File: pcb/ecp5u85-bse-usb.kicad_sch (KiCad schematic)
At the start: 25 parts, among them J1 Conn_02x40_Odd_Even, J2 Conn_02x40_Odd_Even

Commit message: Fix some ERC errors
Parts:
- gave numbers to parts that had none: 23
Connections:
- net +2V5: now also R33.1
- no-connect marks 15 -> 16

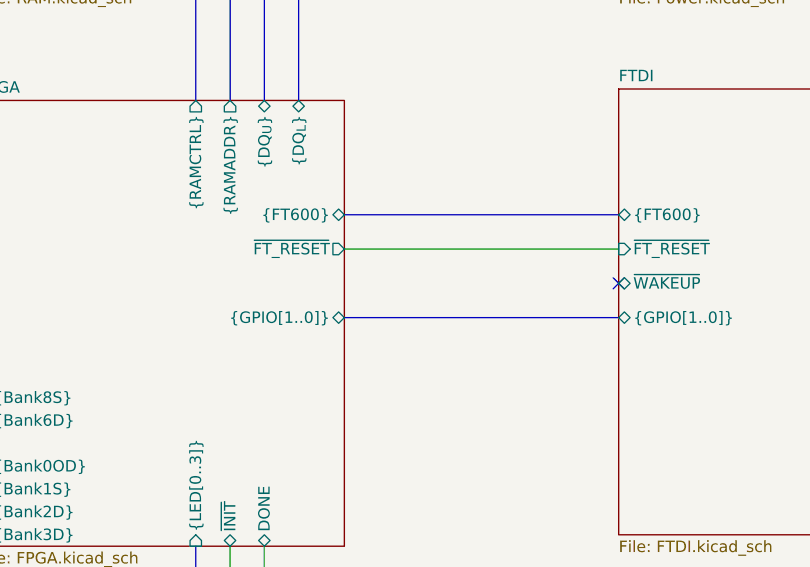
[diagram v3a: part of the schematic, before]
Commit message: Conect FT_WAKEUP and move FT_RESET to an optional circuit
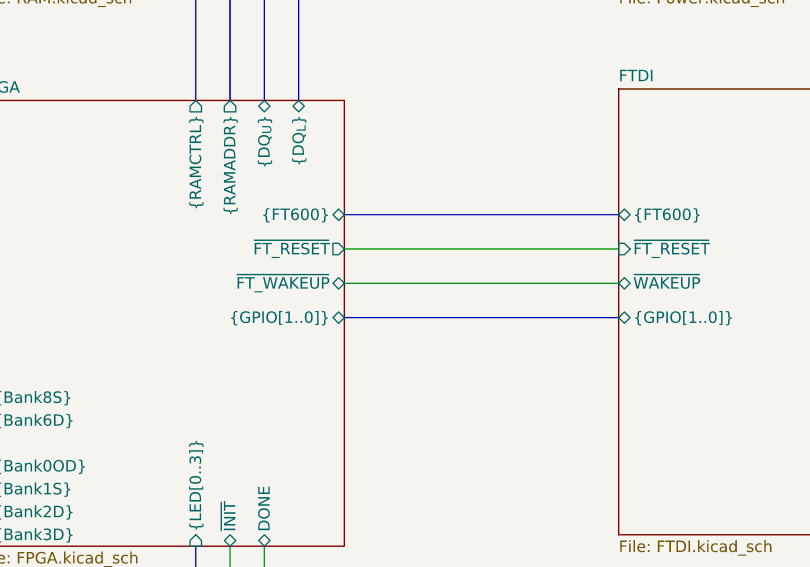
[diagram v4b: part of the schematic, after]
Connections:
- no-connect marks 16 -> 15
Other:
- sheet FPGA ports: added ~{FT_WAKEUP}; removed none
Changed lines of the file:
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@@
   (no_connect (at 124.46 50.8))
   (no_connect (at 50.8 86.36))
-  (no_connect (at 232.41 119.38))
   (no_connect (at 111.76 86.36))
   (no_connect (at 111.76 111.76))
@@
     (stroke (width 0) (type default) (color 0 0 0 0))
   )
+  (wire (pts (xy 201.93 119.38) (xy 232.41 119.38))
+    (stroke (width 0) (type default) (color 0 0 0 0))
+  )
   (wire (pts (xy 116.84 168.91) (xy 116.84 171.45))
     (stroke (width 0) (type default) (color 0 0 0 0))
@@
       (effects (font (size 1.27 1.27)) (justify left))
     )
+    (pin "~{FT_WAKEUP}" bidirectional (at 201.93 119.38 0)
+      (effects (font (size 1.27 1.27)) (justify right))
+    )
   )
   (sheet (at 232.41 36.83) (size 40.64 49.53)
@@
       (reference "#PWR0146") (unit 1) (value "GND") (footprint "")
     )
+    (path "/b14c35da-dd14-4b8d-93a9-00f219a92f41/e0f21527-f424-4e94-85a9-f4d04b580738"
+      (reference "#PWR?") (unit 1) (value "GND") (footprint "")
+    )
     (path "/033d1a03-0224-4be7-bf03-d823040c5124/71521d47-d3a3-467c-b9fc-ee021a2aa1a9"
       (reference "C1") (unit 1) (value "10nF") (footprint "")
@@
       (reference "Q1") (unit 1) (value "2N2222") (footprint "")
     )
+    (path "/b14c35da-dd14-4b8d-93a9-00f219a92f41/f4511b36-efd8-48bf-93ac-7e8ead7d94e9"
+      (reference "Q?") (unit 1) (value "Q_NMOS_GSD") (footprint "")
+    )
     (path "/033d1a03-0224-4be7-bf03-d823040c5124/013d4fe7-edef-47f4-8eb5-b9479cbae8a4"
       (reference "R1") (unit 1) (value "50") (footprint "")
@@
       (reference "R52") (unit 1) (value "DNP") (footprint "")
     )
+    (path "/b14c35da-dd14-4b8d-93a9-00f219a92f41/5d1ea4c5-5a48-430b-8476-099bd47b4f04"
+      (reference "R?") (unit 1) (value "R_US") (footprint "")
+    )
+    (path "/b14c35da-dd14-4b8d-93a9-00f219a92f41/644bc752-376f-4806-81c3-01a41651ba7e"
+      (reference "R?") (unit 1) (value "R_US") (footprint "")
+    )
     (path "/b14c35da-dd14-4b8d-93a9-00f219a92f41/35de3d0a-9421-4407-a409-3752ea1d7831"

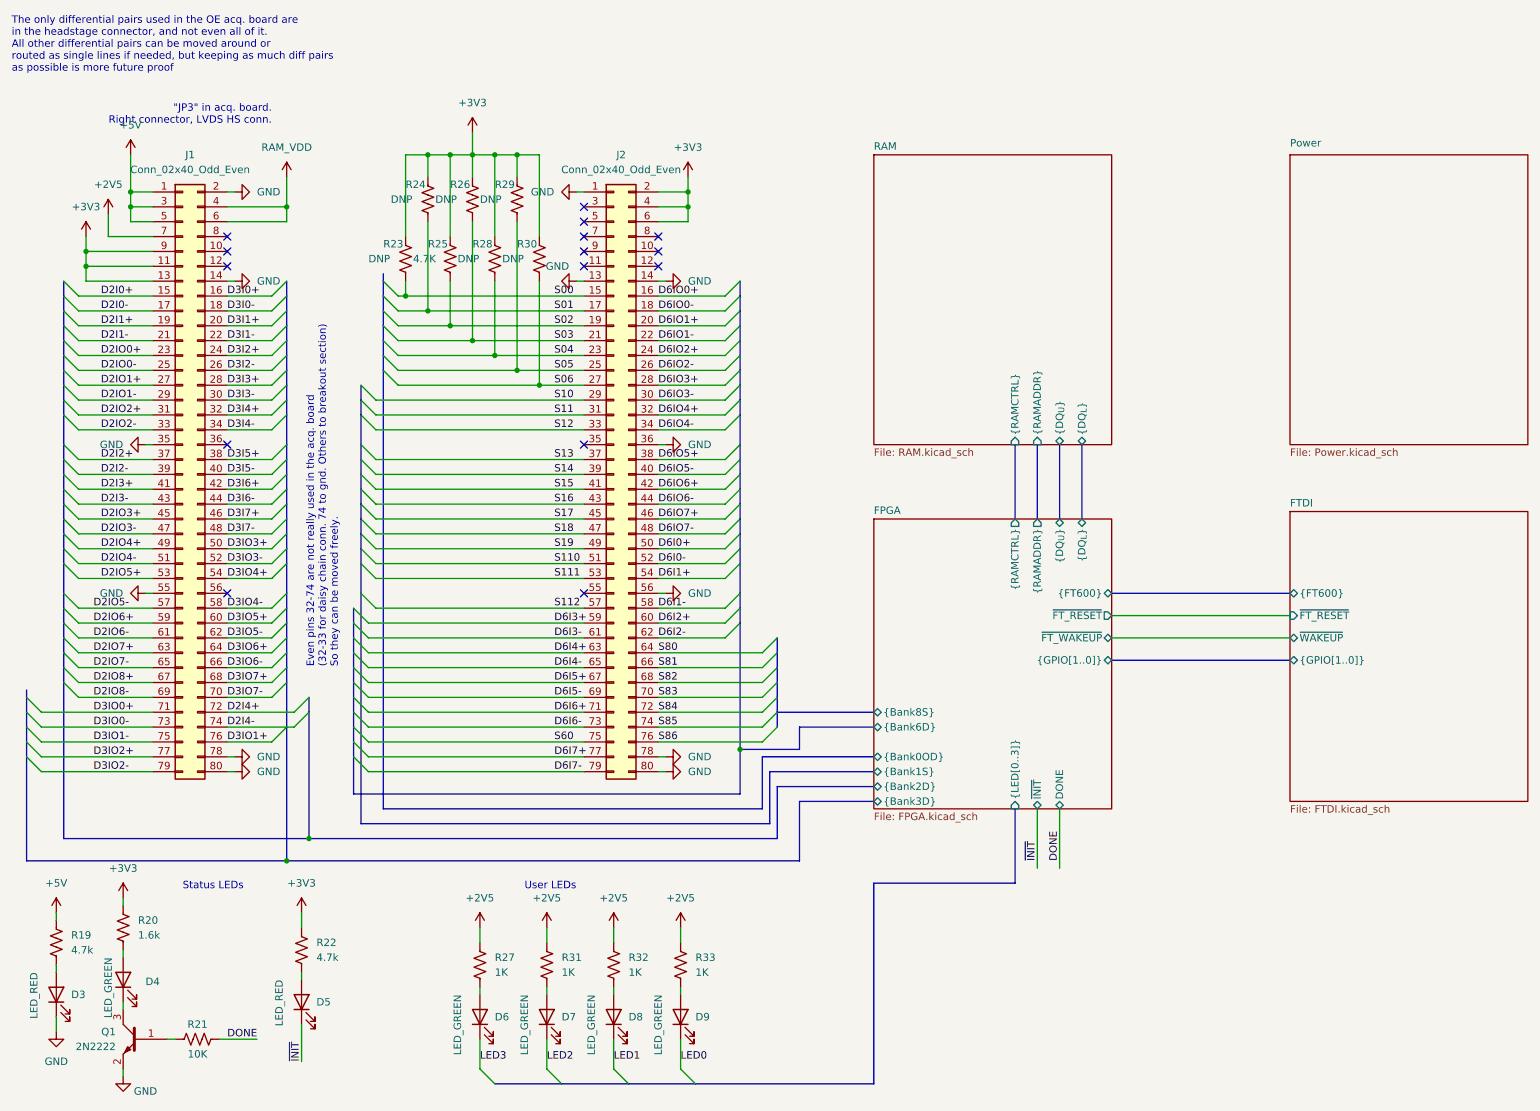
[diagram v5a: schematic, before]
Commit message: Add FPGA oscillator
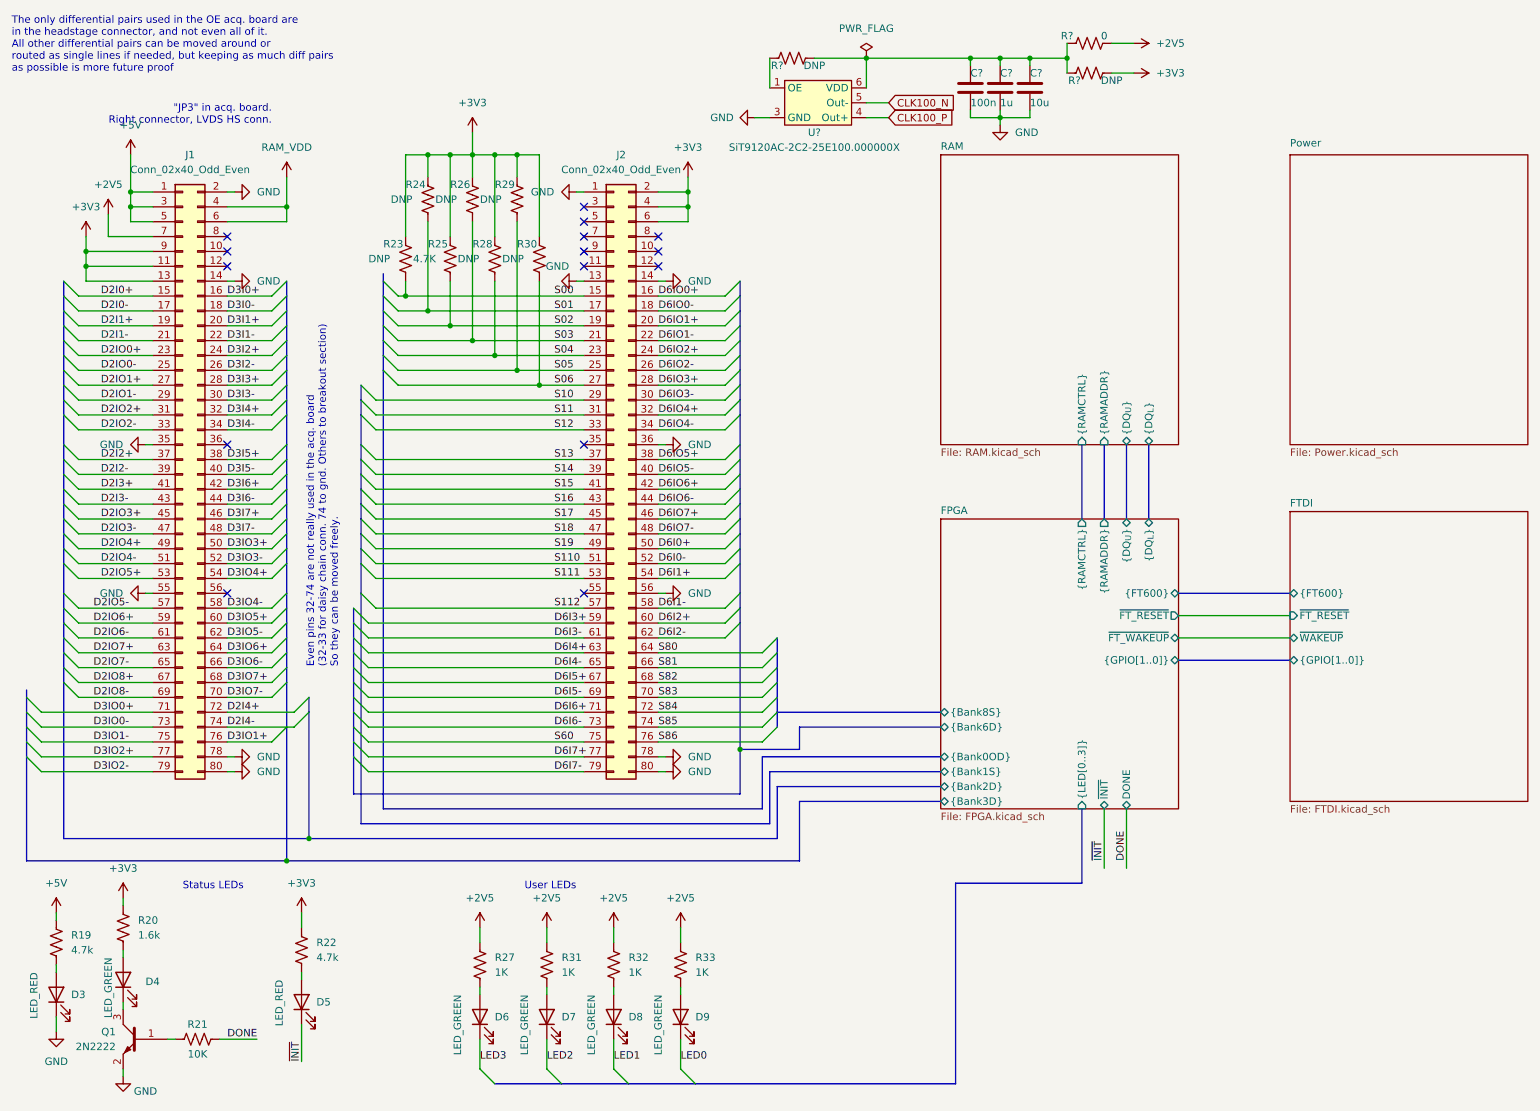
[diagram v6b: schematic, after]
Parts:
- added C?: 1u, symbol Device:C
- added C?: 100n, symbol Device:C
- added C?: 10u, symbol Device:C
- added R? (x2): DNP, symbol Device:R_US
- added R?: 0, symbol Device:R_US
- added U?: SiT9120AC-2C2-25E100.000000X, symbol ecp5u85-bse-usb:OSCILLATOR_DIFF
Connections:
- net +2V5: now also R?.2
- net +3V3: now also R?.2
- net GND: now also C?.2, C?.2, C?.2, U?.3 (GND)
- new net: C?.1, C?.1, C?.1, R?.1, R?.1, R?.2, U?.6 (VDD)
- new net: R?.1, U?.1 (OE)
- new net CLK100_N: U?.5 (Out-)
- new net CLK100_P: U?.4 (Out+)

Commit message: Update libraries
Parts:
- gave numbers to parts that had none: 7
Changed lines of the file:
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@@
   (symbol (lib_id "Device:R_US") (at 198.12 22.86 90) (unit 1)
     (in_bom yes) (on_board yes)
-    (property "Reference" "R?" (id 0) (at 195.58 24.13 90))
+    (property "Reference" "R57" (id 0) (at 195.58 24.13 90))
     (property "Value" "DNP" (id 1) (at 201.93 24.13 90))
     (property "Footprint" "" (id 2) (at 198.374 21.844 90)
@@
   (symbol (lib_id "Device:R_US") (at 147.32 20.32 90) (unit 1)
     (in_bom yes) (on_board yes)
-    (property "Reference" "R?" (id 0) (at 144.78 21.59 90))
+    (property "Reference" "R55" (id 0) (at 144.78 21.59 90))
     (property "Value" "DNP" (id 1) (at 151.13 21.59 90))
     (property "Footprint" "" (id 2) (at 147.574 19.304 90)
@@
   (symbol (lib_id "power:+2V5") (at 205.74 17.78 270) (unit 1)
     (in_bom yes) (on_board yes) (fields_autoplaced)
-    (property "Reference" "#PWR?" (id 0) (at 201.93 17.78 0)
+    (property "Reference" "#PWR086" (id 0) (at 201.93 17.78 0)
       (effects (font (size 1.27 1.27)) hide)
     )
@@
   (symbol (lib_id "Device:C") (at 182.88 25.4 0) (unit 1)
     (in_bom yes) (on_board yes)
-    (property "Reference" "C?" (id 0) (at 182.88 22.86 0)
+    (property "Reference" "C131" (id 0) (at 182.88 22.86 0)
       (effects (font (size 1.27 1.27)) (justify left))
     )
@@
   (symbol (lib_id "Device:R_US") (at 198.12 17.78 90) (unit 1)
     (in_bom yes) (on_board yes)
-    (property "Reference" "R?" (id 0) (at 194.31 16.51 90))
+    (property "Reference" "R56" (id 0) (at 194.31 16.51 90))
     (property "Value" "0" (id 1) (at 200.66 16.51 90))
     (property "Footprint" "" (id 2) (at 198.374 16.764 90)
@@
   (symbol (lib_id "Device:C") (at 177.8 25.4 0) (unit 1)
     (in_bom yes) (on_board yes)
-    (property "Reference" "C?" (id 0) (at 177.8 22.86 0)
+    (property "Reference" "C130" (id 0) (at 177.8 22.86 0)
       (effects (font (size 1.27 1.27)) (justify left))
     )
@@
   (symbol (lib_id "ecp5u85-bse-usb:OSCILLATOR_DIFF") (at 151.13 27.94 0) (unit 1)
     (in_bom yes) (on_board yes)
-    (property "Reference" "U?" (id 0) (at 151.13 33.02 0))
+    (property "Reference" "U10" (id 0) (at 151.13 33.02 0))
     (property "Value" "SiT9120AC-2C2-25E100.000000X" (id 1) (at 151.13 35.56 0))
     (property "Footprint" "" (id 2) (at 151.13 27.94 0)
@@
   (symbol (lib_id "power:GND") (at 182.88 31.75 0) (unit 1)
     (in_bom yes) (on_board yes) (fields_autoplaced)
-    (property "Reference" "#PWR?" (id 0) (at 182.88 38.1 0)
+    (property "Reference" "#PWR085" (id 0) (at 182.88 38.1 0)
       (effects (font (size 1.27 1.27)) hide)
     )
@@
   (symbol (lib_id "Device:C") (at 187.96 25.4 0) (unit 1)
     (in_bom yes) (on_board yes)
-    (property "Reference" "C?" (id 0) (at 187.96 22.86 0)
+    (property "Reference" "C132" (id 0) (at 187.96 22.86 0)
       (effects (font (size 1.27 1.27)) (justify left))
     )
@@
   (symbol (lib_id "power:+3V3") (at 205.74 22.86 270) (unit 1)
     (in_bom yes) (on_board yes) (fields_autoplaced)
-    (property "Reference" "#PWR?" (id 0) (at 201.93 22.86 0)
+    (property "Reference" "#PWR087" (id 0) (at 201.93 22.86 0)
       (effects (font (size 1.27 1.27)) hide)
     )
@@
   (symbol (lib_id "power:GND") (at 140.97 30.48 270) (unit 1)
     (in_bom yes) (on_board yes)
-    (property "Reference" "#PWR?" (id 0) (at 134.62 30.48 0)
+    (property "Reference" "#PWR084" (id 0) (at 134.62 30.48 0)
       (effects (font (size 1.27 1.27)) hide)
     )
@@
   (symbol (lib_id "power:PWR_FLAG") (at 160.02 20.32 0) (unit 1)
     (in_bom yes) (on_board yes) (fields_autoplaced)
-    (property "Reference" "#FLG?" (id 0) (at 160.02 18.415 0)
+    (property "Reference" "#FLG01" (id 0) (at 160.02 18.415 0)
       (effects (font (size 1.27 1.27)) hide)
     )
@@
   )
   (symbol_instances
+    (path "/e3e79ab3-3ac6-45da-9fd8-9391667738c6"
+      (reference "#FLG01") (unit 1) (value "PWR_FLAG") (footprint "")
+    )
     (path "/033d1a03-0224-4be7-bf03-d823040c5124/e7b81188-d5b1-45b6-802a-c5e15290724c"
       (reference "#FLG0101") (unit 1) (value "PWR_FLAG") (footprint "")
@@
       (reference "#FLG0106") (unit 1) (value "PWR_FLAG") (footprint "")
     )
-    (path "/e3e79ab3-3ac6-45da-9fd8-9391667738c6"
-      (reference "#FLG?") (unit 1) (value "PWR_FLAG") (footprint "")
-    )
     (path "/f1efb15c-659a-4f46-a1e2-00583fbf7e18"
       (reference "#PWR01") (unit 1) (value "+5V") (footprint "")
@@
       (reference "#PWR083") (unit 1) (value "GND") (footprint "")
     )
+    (path "/df0ebd3b-9663-4b1a-a601-a7786f15999a"
+      (reference "#PWR084") (unit 1) (value "GND") (footprint "")
+    )
+    (path "/83d4ad53-d443-46e1-9d81-ab90833c2c63"
+      (reference "#PWR085") (unit 1) (value "GND") (footprint "")
+    )
+    (path "/4840610c-b6be-4e19-85ea-ad805e3d3d3e"
+      (reference "#PWR086") (unit 1) (value "+2V5") (footprint "")
+    )
+    (path "/dc950138-6c28-4005-aa75-454f9ffe17c5"
+      (reference "#PWR087") (unit 1) (value "+3V3") (footprint "")
+    )
     (path "/f8db7611-6744-489f-b566-226cb154f69c"
       (reference "#PWR0101") (unit 1) (value "GND") (footprint "")
@@
       (reference "#PWR0146") (unit 1) (value "GND") (footprint "")
     )
-    (path "/4840610c-b6be-4e19-85ea-ad805e3d3d3e"
-      (reference "#PWR?") (unit 1) (value "+2V5") (footprint "")
-    )
-    (path "/83d4ad53-d443-46e1-9d81-ab90833c2c63"
-      (reference "#PWR?") (unit 1) (value "GND") (footprint "")
-    )
-    (path "/dc950138-6c28-4005-aa75-454f9ffe17c5"
-      (reference "#PWR?") (unit 1) (value "+3V3") (footprint "")
-    )
-    (path "/df0ebd3b-9663-4b1a-a601-a7786f15999a"
-      (reference "#PWR?") (unit 1) (value "GND") (footprint "")
-    )
     (path "/033d1a03-0224-4be7-bf03-d823040c5124/71521d47-d3a3-467c-b9fc-ee021a2aa1a9"
       (reference "C1") (unit 1) (value "10nF") (footprint "")
@@
       (reference "C129") (unit 1) (value "100n") (footprint "")
     )
+    (path "/6ab0fe63-f09c-490f-95f3-0cd35104f840"
+      (reference "C130") (unit 1) (value "100n") (footprint "")
+    )
     (path "/4909740b-341d-4706-b9b8-ce34e5275566"
-      (reference "C?") (unit 1) (value "1u") (footprint "")
-    )
-    (path "/6ab0fe63-f09c-490f-95f3-0cd35104f840"
-      (reference "C?") (unit 1) (value "100n") (footprint "")
+      (reference "C131") (unit 1) (value "1u") (footprint "")
     )
     (path "/a48b2080-8987-4ffd-832f-ec1eaf4b8923"
-      (reference "C?") (unit 1) (value "10u") (footprint "")
+      (reference "C132") (unit 1) (value "10u") (footprint "")
     )
     (path "/0d9a5925-3677-4baf-8c3e-88d6199b0d1b/c33df375-2f90-45cf-ae00-c26362646f5f"
@@
       (reference "R54") (unit 1) (value "R_US") (footprint "")
     )
+    (path "/2e62fb67-5691-4868-9df8-29b21153f0c3"
+      (reference "R55") (unit 1) (value "DNP") (footprint "")
+    )
+    (path "/6608ee67-e53f-4db3-a883-c0a0f72e9187"
+      (reference "R56") (unit 1) (value "0") (footprint "")
+    )
     (path "/2531e6f3-7b8e-4573-82c7-65b8b489ed2f"
-      (reference "R?") (unit 1) (value "DNP") (footprint "")
-    )
-    (path "/2e62fb67-5691-4868-9df8-29b21153f0c3"
-      (reference "R?") (unit 1) (value "DNP") (footprint "")
-    )
-    (path "/6608ee67-e53f-4db3-a883-c0a0f72e9187"
-      (reference "R?") (unit 1) (value "0") (footprint "")
+      (reference "R57") (unit 1) (value "DNP") (footprint "")
     )
     (path "/b14c35da-dd14-4b8d-93a9-00f219a92f41/35de3d0a-9421-4407-a409-3752ea1d7831"
@@
     )
     (path "/763496f3-121d-476b-92ed-2928dd374644"
-      (reference "U?") (unit 1) (value "SiT9120AC-2C2-25E100.000000X") (footprint "")
+      (reference "U10") (unit 1) (value "SiT9120AC-2C2-25E100.000000X") (footprint "")
     )
     (path "/0d9a5925-3677-4baf-8c3e-88d6199b0d1b/e633dcce-c429-4e08-91cd-69533e8cfa17"
